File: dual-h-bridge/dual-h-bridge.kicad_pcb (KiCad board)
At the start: 2 copper layers, 40.9 x 101.5 mm, 80 parts, among them J1 Motor0, J2 Motor1, J3 BATT, J4 MCU, M0.Fow_Gate Motor0.FOW_GATE, M0.Rev_Gate Motor0.REV_GATE, M1.Fow_Gate Motor1.FOW_GATE, M1.Rev_Gate Motor1.REV_GATE, Q1 2N3904, Q10 VN2222L, Q11 IRFZ44, Q12 IRFZ44, Q13 2N3904, Q14 VN2222L, Q15 IRFZ44, Q16 IRFZ44, Q17 2N3904, Q18 VN2222L, Q2 2N3904, Q3 IRFZ44, Q4 IRFZ44, Q5 2N3904, Q6 VN2222L, Q7 IRFZ44, Q8 IRFZ44, Q9 2N3904, U1 LT1161, U2 MCT6, U3 MCT6

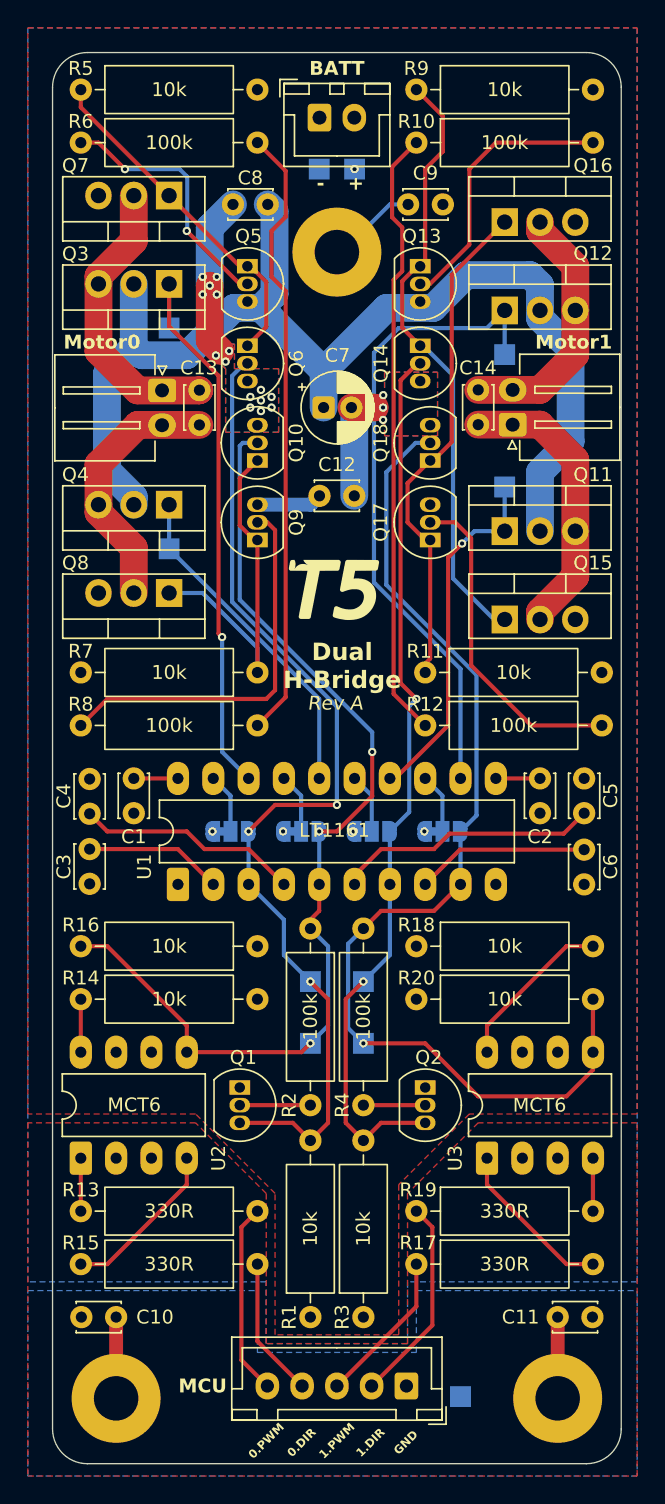
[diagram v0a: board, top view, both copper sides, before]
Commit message: Fix potentially inverted H-Bridge direction bit
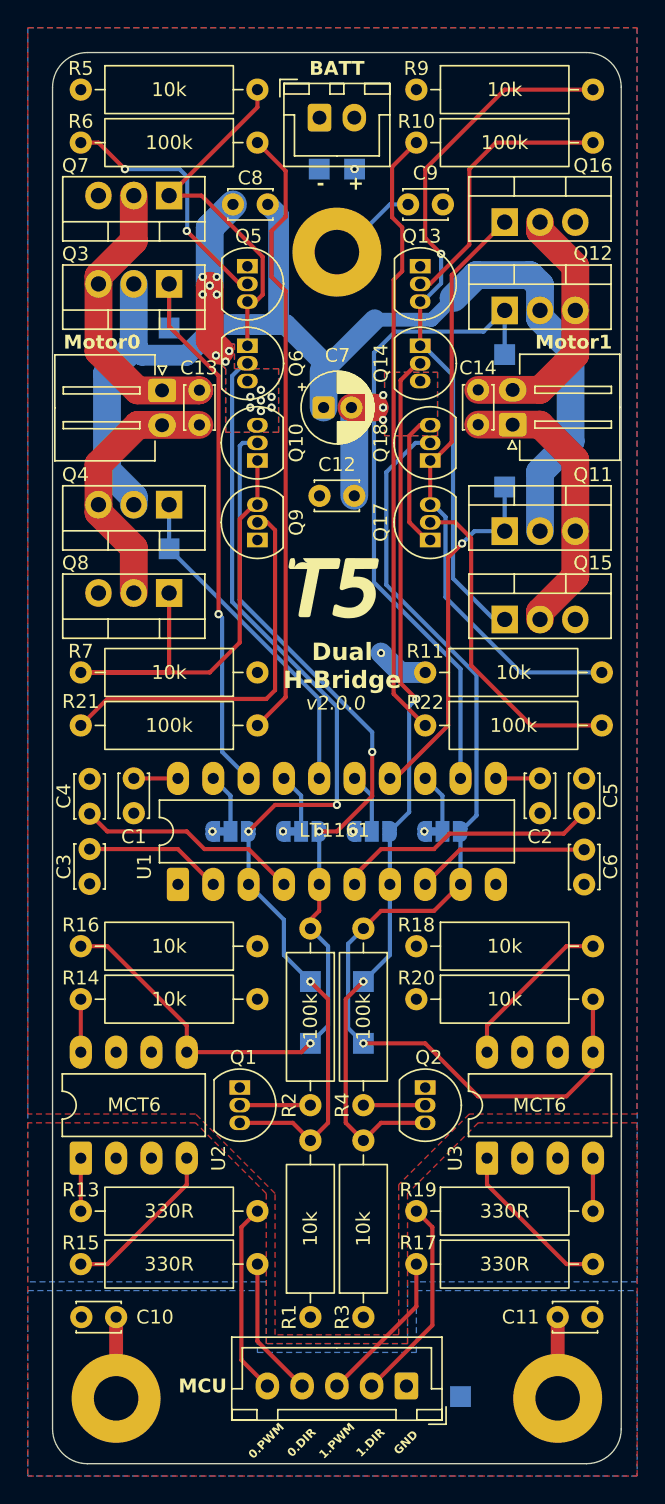
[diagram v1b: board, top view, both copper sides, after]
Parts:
- removed R12, R8: 100k, Resistor_THT:R_Axial_DIN0309_L9.0mm_D3.2mm_P12.70mm_Horizontal
- removed REF**: , GS_Virtual:ENPH253_Logo_Small
- removed REF**: KiCad-Logo2_5mm_SilkScreen, Symbol:KiCad-Logo2_5mm_SilkScreen
- removed REF**: OSHW-Logo_7.5x8mm_SilkScreen, Symbol:OSHW-Logo_7.5x8mm_SilkScreen
- added R21: 100k, Resistor_THT:R_Axial_DIN0309_L9.0mm_D3.2mm_P12.70mm_Horizontal, F.Cu at (207.0, 88.8)
- added R22: 100k, Resistor_THT:R_Axial_DIN0309_L9.0mm_D3.2mm_P12.70mm_Horizontal, F.Cu at (219.1, 88.8)
- added S1: Logo, GS_Virtual:ENPH253_Logo_Small, F.Cu at (212.8, 78.7)
- renumbered ~{DIR0} to JP1, DIR0 to JP2, ~{DIR1} to JP3, DIR1 to JP4, M0.Rev_Gate to TP10, M1.Fow_Gate to TP11, M1.Rev_Gate to TP12, MCU.GND to TP19, ~{DIR0} to TP5, DIR0 to TP6, M0.Fow_Gate to TP7, ~{DIR1} to TP8, DIR1 to TP9
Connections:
- Q13 pad 1: /H-Bridge 1/REV_LOW_GATE -> GNDPWR
- Q13 pad 3: +BATT -> /H-Bridge 1/REV_LOW_GATE
- Q17 pad 1: /H-Bridge 1/FOW_LOW_GATE -> GNDPWR
- Q17 pad 3: +BATT -> /H-Bridge 1/FOW_LOW_GATE
- Q5 pad 1: /H-Bridge 0/REV_LOW_GATE -> GNDPWR
- Q5 pad 3: +BATT -> /H-Bridge 0/REV_LOW_GATE
- Q9 pad 1: /H-Bridge 0/FOW_LOW_GATE -> GNDPWR
- Q9 pad 3: +BATT -> /H-Bridge 0/FOW_LOW_GATE
- R11 pad 1: /H-Bridge 1/FOW_LOW_GATE -> +BATT
- R11 pad 2: GNDPWR -> /H-Bridge 1/FOW_LOW_GATE
- R5 pad 1: /H-Bridge 0/REV_LOW_GATE -> +BATT
- R5 pad 2: GNDPWR -> /H-Bridge 0/REV_LOW_GATE
- R7 pad 1: /H-Bridge 0/FOW_LOW_GATE -> +BATT
- R7 pad 2: GNDPWR -> /H-Bridge 0/FOW_LOW_GATE
- R9 pad 1: /H-Bridge 1/REV_LOW_GATE -> +BATT
- R9 pad 2: GNDPWR -> /H-Bridge 1/REV_LOW_GATE
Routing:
- net GNDPWR: track 21.4 -> 33.5 mm
- net /H-Bridge 0/FOW_LOW_GATE: track 26.2 -> 38.1 mm
- net /H-Bridge 1/REV_LOW_GATE: track 43.9 -> 51.1 mm, vias 0 -> 1
- net /H-Bridge 1/FOW_LOW_GATE: track 36.4 -> 43.4 mm
- net +BATT: track 94.7 -> 96.1 mm, vias 5 -> 6
- net /H-Bridge 0/REV_LOW_GATE: track 25.0 -> 26.0 mm
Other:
- board text added: "v2.0.0"
- board text removed: "Rev A"

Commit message: Update silkscreen
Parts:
- added REF**: KiCad-Logo2_6mm_SilkScreen, Symbol:KiCad-Logo2_6mm_SilkScreen, B.Cu at (212.7, 79.4)
- added REF**: OSHW-Logo_7.5x8mm_SilkScreen, Symbol:OSHW-Logo_7.5x8mm_SilkScreen, B.Cu at (224.8, 46.4)
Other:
- board text added: "v2.0.1"
- board text removed: "v2.0.0"

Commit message: Fix optocoupler hardware issue
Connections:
- R10 pad 1: /PWM1 -> /Motor1.PWM
- R14 pad 1: GNDPWR -> /Motor0.PWM
- R14 pad 2: /Motor0.PWM -> +BATT
- R18 pad 1: GNDPWR -> /Motor1.PWM
- R18 pad 2: /Motor1.PWM -> +BATT
- R21 pad 1: /PWM0 -> /Motor0.PWM
- R22 pad 1: /PWM1 -> /Motor1.PWM
- R6 pad 1: /PWM0 -> /Motor0.PWM
- U2 pad 7: +BATT -> /Motor0.PWM
- U2 pad 8: /Motor0.PWM -> GNDPWR
- U3 pad 7: +BATT -> /Motor1.PWM
- U3 pad 8: /Motor1.PWM -> GNDPWR
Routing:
- net /Motor0.PWM: track 3.81 -> 88.9 mm, vias 0 -> 1
- net /Motor1.PWM: track 11.9 -> 89.5 mm, vias 0 -> 2
- net /PWM0: track 44.4 -> 0.00 mm
- net /PWM1: track 44.1 -> 0.00 mm
- net +BATT: track 96.1 -> 111.4 mm
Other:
- board text added: "${REVISION}"
- board text removed: "v2.0.1"

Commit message: Some small updates
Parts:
- R1, R11, R14, R16, R18, R20, R3, R5, R7, R9: value 10k -> 1k
- R10, R2, R21, R22, R4, R6: value 100k -> 10k
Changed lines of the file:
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@@
 		(title "Dual H-Bridge")
 		(date "2025-07-09")
-		(rev "v3.0.0")
+		(rev "v3.0.1")
 		(company "Team 5")
 		(comment 1 "George Sleen")
@@
 			)
 		)
-		(property "Value" "10k"
+		(property "Value" "1k"
 			(at 6.35 0 0)
 			(layer "F.SilkS")
@@
 			)
 		)
-		(property "Value" "10k"
+		(property "Value" "1k"
 			(at 6.35 0 0)
 			(layer "F.SilkS")
@@
 			)
 		)
-		(property "Value" "100k"
+		(property "Value" "10k"
 			(at 6.35 0 90)
 			(layer "F.SilkS")
@@
 			)
 		)
-		(property "Value" "10k"
+		(property "Value" "1k"
 			(at 6.35 0 90)
 			(layer "F.SilkS")
@@
 			)
 		)
-		(property "Value" "100k"
+		(property "Value" "10k"
 			(at 6.35 0 0)
 			(layer "F.SilkS")
@@
 			)
 		)
-		(property "Value" "10k"
+		(property "Value" "1k"
 			(at 6.35 0 0)
 			(layer "F.SilkS")
@@
 			)
 		)
-		(property "Value" "100k"
+		(property "Value" "10k"
 			(at 6.35 0 0)
 			(layer "F.SilkS")
@@
 			)
 		)
-		(property "Value" "100k"
+		(property "Value" "10k"
 			(at 6.35 0 0)
 			(layer "F.SilkS")
@@
 			)
 		)
-		(property "Value" "10k"
+		(property "Value" "1k"
 			(at 6.35 0 0)
 			(layer "F.SilkS")
@@
 			)
 		)
-		(property "Value" "10k"
+		(property "Value" "1k"
 			(at 6.35 0 0)
 			(layer "F.SilkS")
@@
 			)
 		)
-		(property "Value" "10k"
+		(property "Value" "1k"
 			(at 6.35 0 0)
 			(layer "F.SilkS")
@@
 			)
 		)
-		(property "Value" "10k"
+		(property "Value" "1k"
 			(at 6.35 0 0)
 			(layer "F.SilkS")
@@
 			)
 		)
-		(property "Value" "10k"
+		(property "Value" "1k"
 			(at 6.35 0 90)
 			(layer "F.SilkS")
@@
 			)
 		)
-		(property "Value" "10k"
+		(property "Value" "1k"
 			(at 6.35 0 0)
 			(layer "F.SilkS")
@@
 			)
 		)
-		(property "Value" "100k"
+		(property "Value" "10k"
 			(at 6.35 0 0)
 			(layer "F.SilkS")
@@
 			)
 		)
-		(property "Value" "100k"
+		(property "Value" "10k"
 			(at 6.35 0 90)
 			(layer "F.SilkS")

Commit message: Fix all hardware issues and generate final release source files
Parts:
- added TP12: Motor0.PWM, TestPoint:TestPoint_Pad_1.5x1.5mm, B.Cu at (200.7, 85.1)
- added TP13: Motor1.PWM, TestPoint:TestPoint_Pad_1.5x1.5mm, B.Cu at (225.6, 85.1)
- R1, R11, R3, R5, R7, R9: value 1k -> 10k
- R10, R6: value 10k -> 100k
- R12: renamed from R22; value 10k -> 100k
- R13: renamed from R14; value 1k -> 10k
- R15: renamed from R16; value 1k -> 10k
- R17: renamed from R18; value 1k -> 10k
- R19: renamed from R20; value 1k -> 10k
- R8: renamed from R21; value 10k -> 100k
- renumbered C9 to C10, C10 to C11, C11 to C12, C12 to C9, J4 to J2, J2 to J3, J3 to J4, Q14 to Q13, Q13 to Q14, Q6 to Q5, Q5 to Q6, R13 to R14, R15 to R16, R17 to R18, R19 to R20, TP5 to TP1, TP18 to TP10, TP19 to TP11, TP6 to TP2, TP7 to TP3, TP8 to TP4, TP9 to TP5, TP10 to TP6, TP11 to TP7, TP12 to TP8, TP17 to TP9
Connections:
- R15 pad 1: GNDPWR -> /Motor0.DIR
- R15 pad 2: /Motor0.DIR -> +BATT
- R19 pad 1: GNDPWR -> /Motor1.DIR
- R19 pad 2: /Motor1.DIR -> +BATT
- U2 pad 5: /Motor0.DIR -> GNDPWR
- U2 pad 6: +BATT -> /Motor0.DIR
- U3 pad 5: /Motor1.DIR -> GNDPWR
- U3 pad 6: +BATT -> /Motor1.DIR
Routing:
- net +BATT: track 111.4 -> 96.1 mm
- net /Motor1.DIR: track 78.3 -> 71.2 mm
- net /Motor0.DIR: track 72.9 -> 67.0 mm, vias 3 -> 2
- net /Motor0.PWM: track 88.9 -> 93.6 mm
- net /Motor1.PWM: track 89.5 -> 93.7 mm

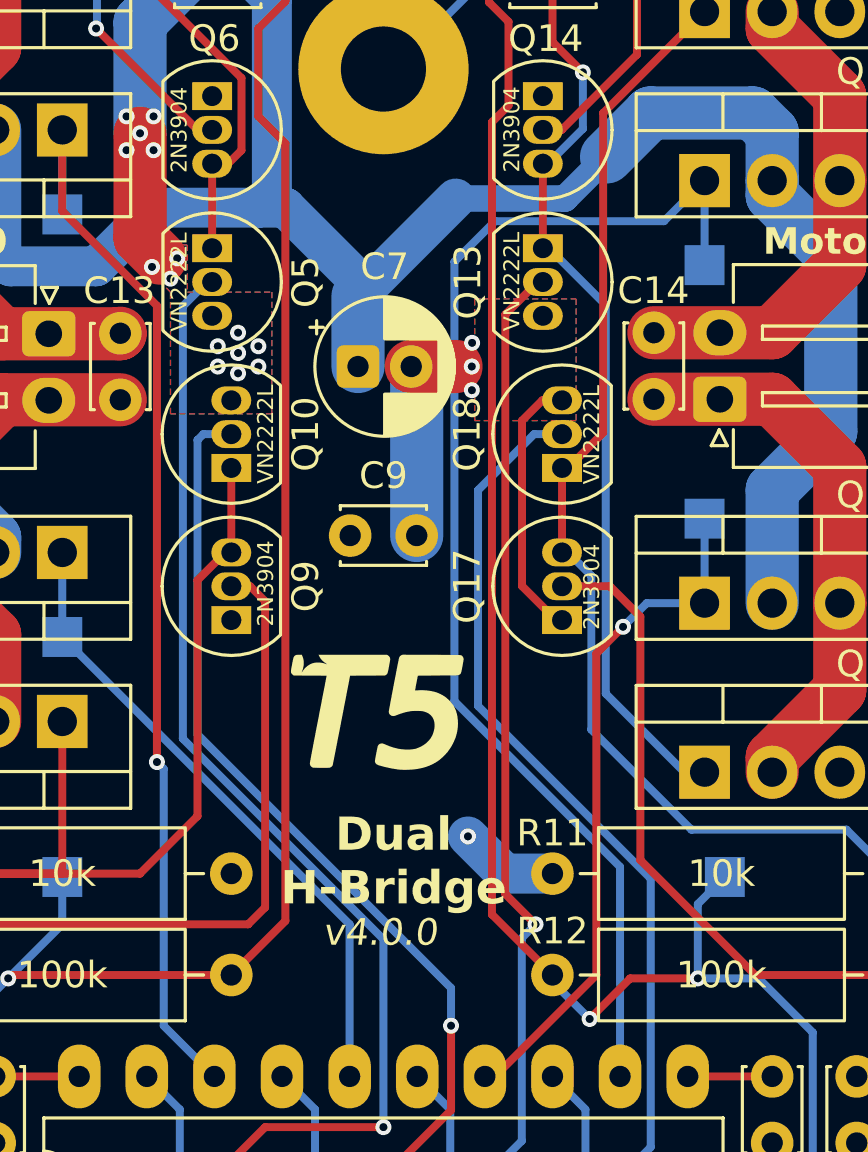
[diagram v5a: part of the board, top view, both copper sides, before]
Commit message: Fix source and drain being swapped on small signal mosfet
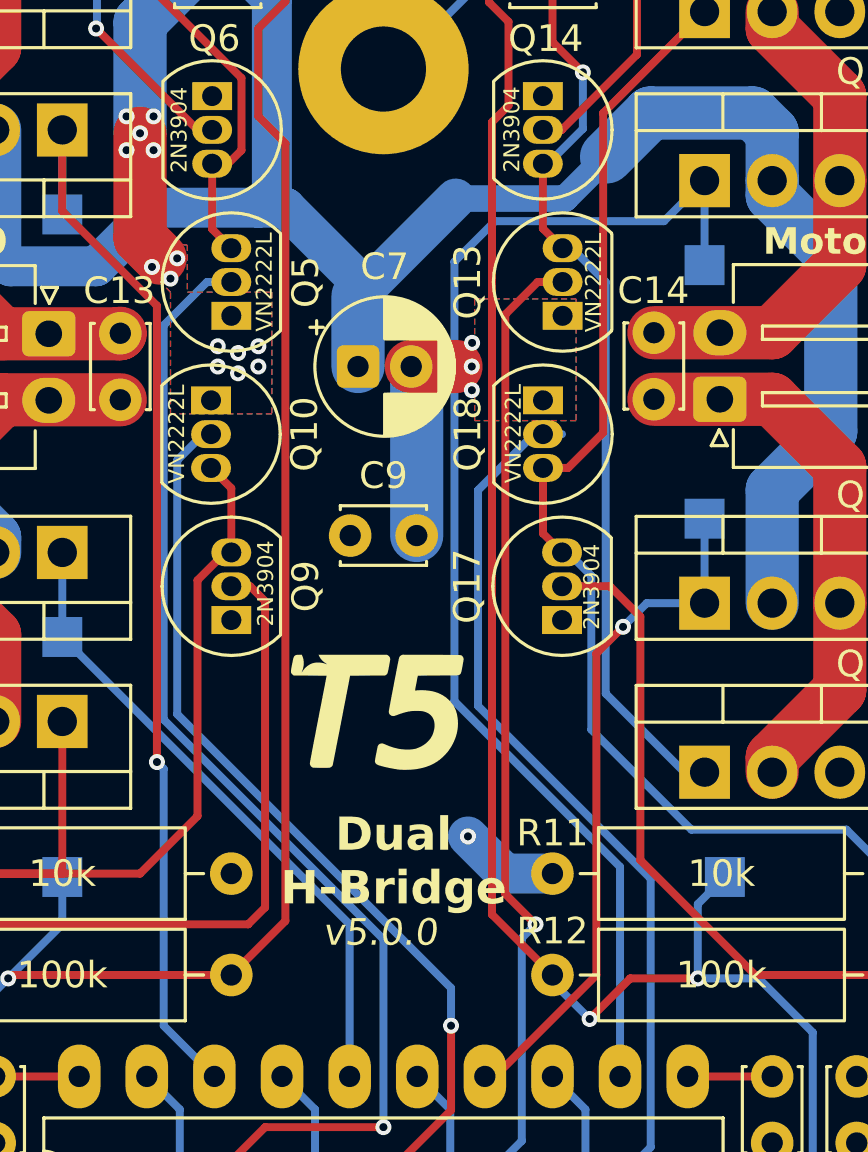
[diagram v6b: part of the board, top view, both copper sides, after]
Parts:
- moved Q10 2.65 mm to (206.2, 67.2), turned to -90 degrees
- moved Q13 2.65 mm to (219.5, 64.0), turned to 90 degrees
- moved Q5 2.64 mm to (207.0, 64.0), turned to 90 degrees
- moved Q18 2.64 mm to (218.7, 67.2), turned to -90 degrees
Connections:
- Q10 pad 1: /H-Bridge 0/FOW_LOW_GATE -> GNDPWR
- Q10 pad 3: GNDPWR -> /H-Bridge 0/FOW_LOW_GATE
- Q13 pad 1: /H-Bridge 1/REV_LOW_GATE -> GNDPWR
- Q13 pad 3: GNDPWR -> /H-Bridge 1/REV_LOW_GATE
- Q18 pad 1: /H-Bridge 1/FOW_LOW_GATE -> GNDPWR
- Q18 pad 3: GNDPWR -> /H-Bridge 1/FOW_LOW_GATE
- Q5 pad 1: /H-Bridge 0/REV_LOW_GATE -> GNDPWR
- Q5 pad 3: GNDPWR -> /H-Bridge 0/REV_LOW_GATE
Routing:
- net GNDPWR: track 33.5 -> 23.7 mm, vias 18 -> 17
- net /H-Bridge 1/FOW_LOW_GATE: track 43.4 -> 44.4 mm
- net /Motor0.~{DIR}: track 73.3 -> 73.9 mm
